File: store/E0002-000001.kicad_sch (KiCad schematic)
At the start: 27 parts, among them J1 Power_IN, J2 Connector, J3 S0 input from DIN meter, J4 Leak sensor, J5 Door reed (NO), J6 Seansor_Header_A, J7 Seansor_Header_B, U1 TMP117xxDRV, U2 INA226

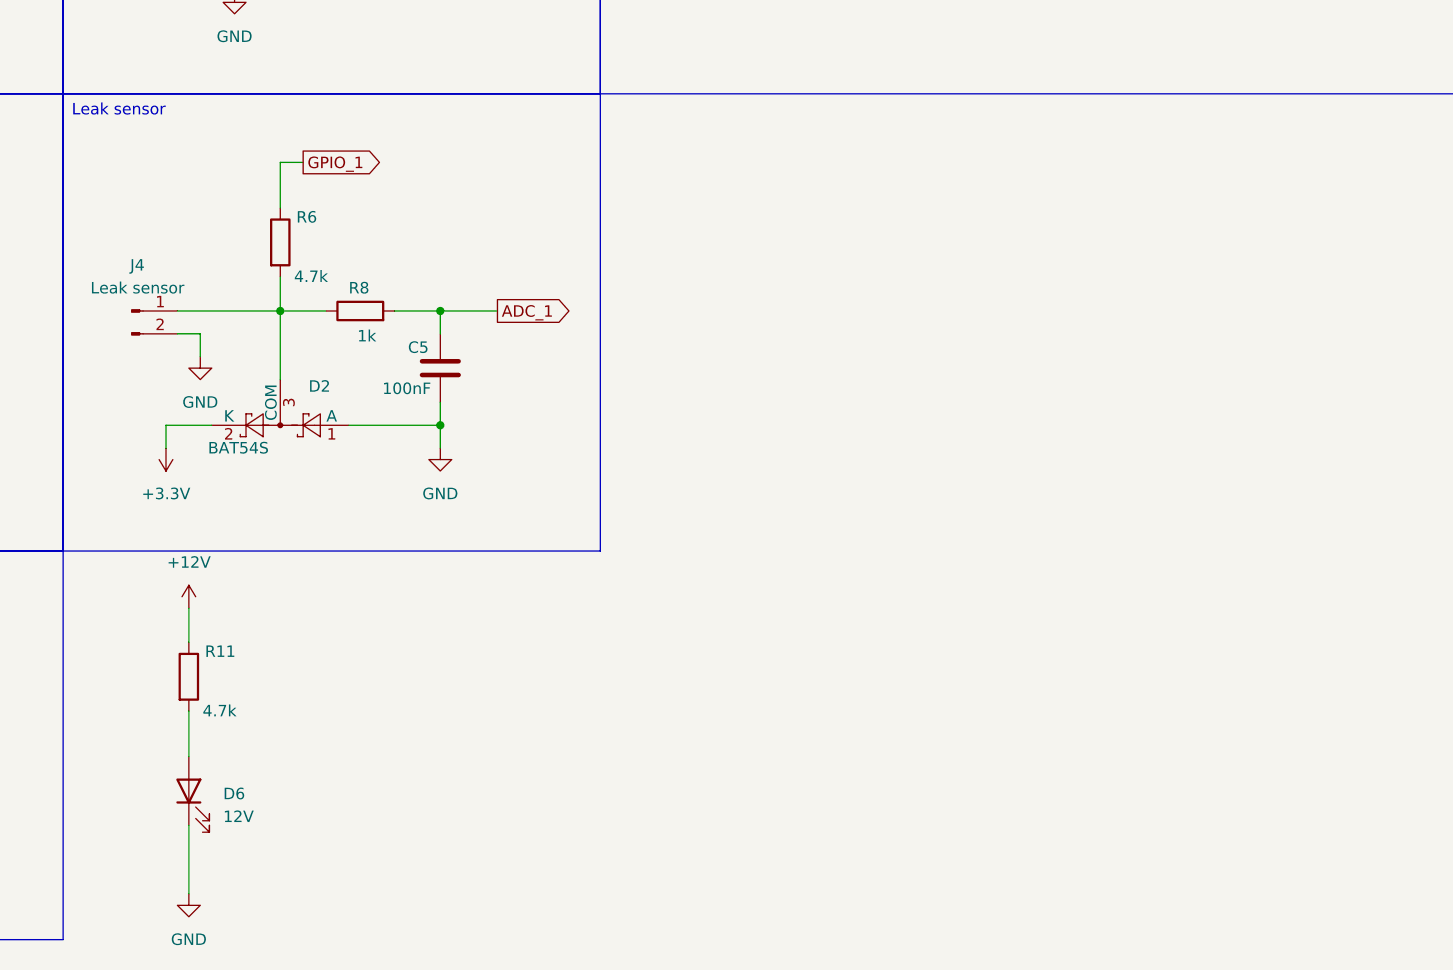
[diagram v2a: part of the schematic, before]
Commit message: feat(E0002): continue PCB layout and add footprint library table
- Update E0002 PCB layout, schematic, and project routing/designators
- Add store/fp-lib-table referencing the industrygrow footprint library
- Update active layer state in E0001/E0002 board settings

Signed-off-by: IIchukissII <133657307+IIchukissII@users.noreply.github.com>
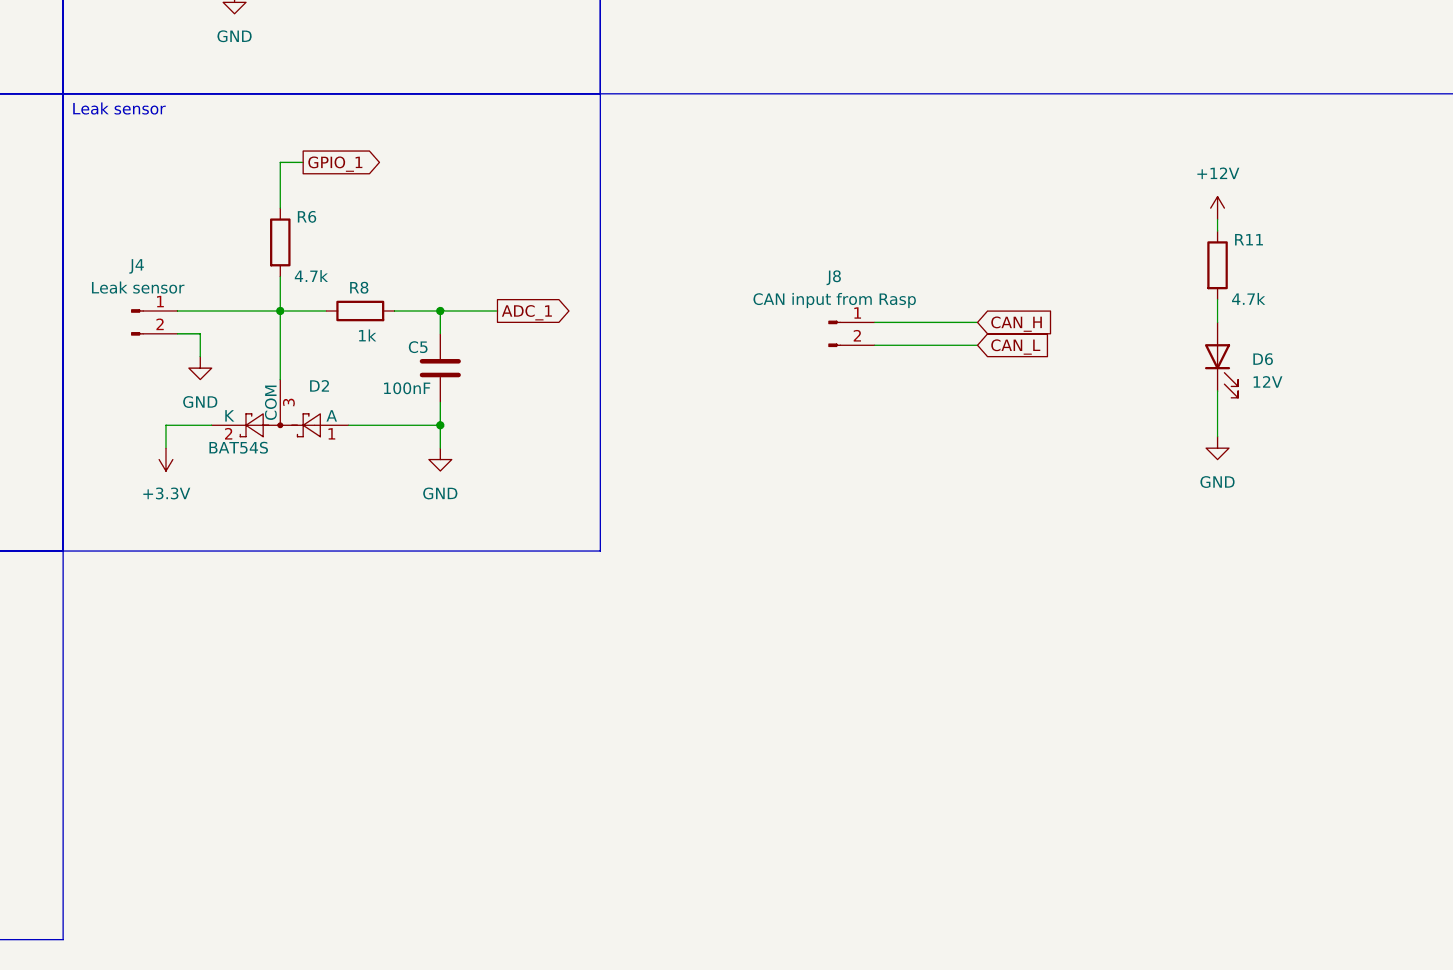
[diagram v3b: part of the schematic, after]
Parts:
- added J8: CAN input from Rasp, TerminalBlock_Phoenix:TerminalBlock_Phoenix_MKDS-1,5-2_1x02_P5.00mm_Horizontal, symbol Connector:Conn_01x02_Pin
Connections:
- net CAN_H: now also J8.1 (Pin_1)
- net CAN_L: now also J8.2 (Pin_2)
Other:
- moved on the sheet: D6, R11
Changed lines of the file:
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@@
 	(wire
 		(pts
-			(xy 133.35 147.32) (xy 133.35 152.4)
+			(xy 247.65 101.6) (xy 247.65 104.14)
 		)
 		(stroke
@@
 	(wire
 		(pts
-			(xy 133.35 135.89) (xy 133.35 139.7)
+			(xy 247.65 92.71) (xy 247.65 93.98)
 		)
 		(stroke
@@
 	(wire
 		(pts
+			(xy 209.55 104.14) (xy 220.98 104.14)
+		)
+		(stroke
+			(width 0)
+			(type default)
+		)
+	)
+	(wire
+		(pts
 			(xy 82.55 153.67) (xy 92.71 153.67)
 		)
@@
 	(wire
 		(pts
-			(xy 133.35 160.02) (xy 133.35 167.64)
+			(xy 247.65 111.76) (xy 247.65 116.84)
 		)
 		(stroke
@@
 	(wire
 		(pts
+			(xy 209.55 106.68) (xy 220.98 106.68)
+		)
+		(stroke
+			(width 0)
+			(type default)
+		)
+	)
+	(wire
+		(pts
 			(xy 81.28 25.4) (xy 81.28 26.67)
 		)
@@
 		)
 	)
+	(global_label "CAN_L"
+		(shape input)
+		(at 220.98 106.68 0)
+		(fields_autoplaced yes)
+		(effects
+			(font
+				(size 1.27 1.27)
+			)
+			(justify left)
+		)
+		(property "Intersheetrefs" "${INTERSHEET_REFS}"
+			(at 229.65 106.68 0)
+			(hide yes)
+			(show_name no)
+			(do_not_autoplace no)
+			(effects
+				(font
+					(size 1.27 1.27)
+				)
+				(justify left)
+			)
+		)
+	)
 	(global_label "I2C1_SDA"
 		(shape output)
@@
 		)
 	)
+	(global_label "CAN_H"
+		(shape input)
+		(at 220.98 104.14 0)
+		(fields_autoplaced yes)
+		(effects
+			(font
+				(size 1.27 1.27)
+			)
+			(justify left)
+		)
+		(property "Intersheetrefs" "${INTERSHEET_REFS}"
+			(at 229.9524 104.14 0)
+			(hide yes)
+			(show_name no)
+			(do_not_autoplace no)
+			(effects
+				(font
+					(size 1.27 1.27)
+				)
+				(justify left)
+			)
+		)
+	)
 	(global_label "I2C1_SCL"
 		(shape output)
@@
 	)
 	(symbol
+		(lib_id "Connector:Conn_01x02_Pin")
+		(at 204.47 104.14 0)
+		(unit 1)
+		(body_style 1)
+		(exclude_from_sim no)
+		(in_bom yes)
+		(on_board yes)
+		(in_pos_files yes)
+		(dnp no)
+		(fields_autoplaced yes)
+		(property "Reference" "J8"
+			(at 205.105 99.06 0)
+			(show_name no)
+			(do_not_autoplace no)
+			(effects
+				(font
+					(size 1.27 1.27)
+				)
+			)
+		)
+		(property "Value" "CAN input from Rasp"
+			(at 205.105 101.6 0)
+			(show_name no)
+			(do_not_autoplace no)
+			(effects
+				(font
+					(size 1.27 1.27)
+				)
+			)
+		)
+		(property "Footprint" "TerminalBlock_Phoenix:TerminalBlock_Phoenix_MKDS-1,5-2_1x02_P5.00mm_Horizontal"
+			(at 204.47 104.14 0)
+			(hide yes)
+			(show_name no)
+			(do_not_autoplace no)
+			(effects
+				(font
+					(size 1.27 1.27)
+				)
+			)
+		)
+		(property "Datasheet" ""
+			(at 204.47 104.14 0)
+			(hide yes)
+			(show_name no)
+			(do_not_autoplace no)
+			(effects
+				(font
+					(size 1.27 1.27)
+				)
+			)
+		)
+		(property "Description" "Generic connector, single row, 01x02, script generated"
+			(at 204.47 104.14 0)
+			(hide yes)
+			(show_name no)
+			(do_not_autoplace no)
+			(effects
+				(font
+					(size 1.27 1.27)
+				)
+			)
+		)
+		(pin "1"
+		)
+		(pin "2"
+		)
+		(instances
+			(project "E0002-000001"
+				(path "/05ff86a2-bfad-446c-a3c5-38b9f5c2eac9"
+					(reference "J8")
+					(unit 1)
+				)
+			)
+		)
+	)
+	(symbol
 		(lib_id "Device:R")
 		(at 143.51 95.25 0)
@@
 	(symbol
 		(lib_id "Device:R")
-		(at 133.35 143.51 0)
+		(at 247.65 97.79 0)
 		(unit 1)
 		(body_style 1)
@@
 		(dnp no)
 		(property "Reference" "R11"
-			(at 135.128 140.716 0)
+			(at 249.428 94.996 0)
 			(show_name no)
 			(do_not_autoplace no)
@@
 		)
 		(property "Value" "4.7k"
-			(at 134.874 147.32 0)
+			(at 249.174 101.6 0)
 			(show_name no)
 			(do_not_autoplace no)
@@
 		)
 		(property "Footprint" "Resistor_SMD:R_0805_2012Metric"
-			(at 131.572 143.51 90)
+			(at 245.872 97.79 90)
 			(hide yes)
 			(show_name no)
@@
 		)
 		(property "Datasheet" ""
-			(at 133.35 143.51 0)
+			(at 247.65 97.79 0)
 			(hide yes)
 			(show_name no)
@@
 		)
 		(property "Description" "Resistor"
-			(at 133.35 143.51 0)
+			(at 247.65 97.79 0)
 			(hide yes)
 			(show_name no)
@@
 	(symbol
 		(lib_id "power:GND")
-		(at 133.35 167.64 0)
+		(at 247.65 116.84 0)
 		(unit 1)
 		(body_style 1)
@@
 		(fields_autoplaced yes)
 		(property "Reference" "#PWR035"
-			(at 133.35 173.99 0)
+			(at 247.65 123.19 0)
 			(hide yes)
 			(show_name no)
@@
 		)
 		(property "Value" "GND"
-			(at 133.35 172.72 0)
+			(at 247.65 121.92 0)
 			(show_name no)
 			(do_not_autoplace no)
@@
 		)
 		(property "Footprint" ""
-			(at 133.35 167.64 0)
+			(at 247.65 116.84 0)
 			(hide yes)
 			(show_name no)
@@
 		)
 		(property "Datasheet" ""
-			(at 133.35 167.64 0)
+			(at 247.65 116.84 0)
 			(hide yes)
 			(show_name no)
@@
 		)
 		(property "Description" "Power symbol creates a global label with name \"GND\" , ground"
-			(at 133.35 167.64 0)
+			(at 247.65 116.84 0)
 			(hide yes)
 			(show_name no)
@@
 	(symbol
 		(lib_id "Device:LED")
-		(at 133.35 156.21 90)
+		(at 247.65 107.95 90)
 		(unit 1)
 		(body_style 1)
@@
 		(fields_autoplaced yes)
 		(property "Reference" "D6"
-			(at 137.16 156.5274 90)
+			(at 251.46 108.2674 90)
 			(show_name no)
 			(do_not_autoplace no)
@@
 		)
 		(property "Value" "12V"
-			(at 137.16 159.0674 90)
+			(at 251.46 110.8074 90)
 			(show_name no)
 			(do_not_autoplace no)
@@
 		)
 		(property "Footprint" "LED_SMD:LED_0805_2012Metric"
-			(at 133.35 156.21 0)
+			(at 247.65 107.95 0)
 			(hide yes)
 			(show_name no)
@@
 		)
 		(property "Datasheet" ""
-			(at 133.35 156.21 0)
+			(at 247.65 107.95 0)
 			(hide yes)
 			(show_name no)
@@
 		)
 		(property "Description" "Light emitting diode"
-			(at 133.35 156.21 0)
+			(at 247.65 107.95 0)
 			(hide yes)
 			(show_name no)
@@
 		)
 		(property "Sim.Pins" "1=K 2=A"
-			(at 133.35 156.21 0)
+			(at 247.65 107.95 0)
 			(hide yes)
 			(show_name no)
@@
 	(symbol
 		(lib_id "power:+12V")
-		(at 133.35 135.89 0)
+		(at 247.65 92.71 0)
 		(unit 1)
 		(body_style 1)
@@
 		(fields_autoplaced yes)
 		(property "Reference" "#PWR033"
-			(at 133.35 139.7 0)
+			(at 247.65 96.52 0)
 			(hide yes)
 			(show_name no)
@@
 		)
 		(property "Value" "+12V"
-			(at 133.35 130.81 0)
+			(at 247.65 87.63 0)
 			(show_name no)
 			(do_not_autoplace no)
@@
 		)
 		(property "Footprint" ""
-			(at 133.35 135.89 0)
+			(at 247.65 92.71 0)
 			(hide yes)
 			(show_name no)
@@
 		)
 		(property "Datasheet" ""
-			(at 133.35 135.89 0)
+			(at 247.65 92.71 0)
 			(hide yes)
 			(show_name no)
@@
 		)
 		(property "Description" "Power symbol creates a global label with name \"+12V\""
-			(at 133.35 135.89 0)
+			(at 247.65 92.71 0)
 			(hide yes)
 			(show_name no)

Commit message: feat(E0002): continue PCB layout and add GND on schematic
Signed-off-by: IIchukissII <133657307+IIchukissII@users.noreply.github.com>
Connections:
- net +3.3V: no longer U2.7 (GND)
- net GND: now also U2.7 (GND)
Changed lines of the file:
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@@
 	(wire
 		(pts
-			(xy 81.28 64.77) (xy 95.25 64.77)
-		)
-		(stroke
-			(width 0)
-			(type default)
-		)
-	)
-	(wire
-		(pts
 			(xy 91.44 48.26) (xy 102.87 48.26)
 		)
@@
 	(wire
 		(pts
-			(xy 81.28 58.42) (xy 81.28 64.77)
+			(xy 81.28 58.42) (xy 81.28 67.31)
 		)
 		(stroke
@@
 					(unit 1)
 				)
+			)
+		)
+	)
+	(symbol
+		(lib_id "power:GND")
+		(at 81.28 67.31 0)
+		(unit 1)
+		(body_style 1)
+		(exclude_from_sim no)
+		(in_bom yes)
+		(on_board yes)
+		(in_pos_files yes)
+		(dnp no)
+		(fields_autoplaced yes)
+		(property "Reference" "#PWR030"
+			(at 81.28 73.66 0)
+			(hide yes)
+			(show_name no)
+			(do_not_autoplace no)
+			(effects
+				(font
+					(size 1.27 1.27)
+				)
+			)
+		)
+		(property "Value" "GND"
+			(at 81.28 72.39 0)
+			(show_name no)
+			(do_not_autoplace no)
+			(effects
+				(font
+					(size 1.27 1.27)
+				)
+			)
+		)
+		(property "Footprint" ""
+			(at 81.28 67.31 0)
+			(hide yes)
+			(show_name no)
+			(do_not_autoplace no)
+			(effects
+				(font
+					(size 1.27 1.27)
+				)
+			)
+		)
+		(property "Datasheet" ""
+			(at 81.28 67.31 0)
+			(hide yes)
+			(show_name no)
+			(do_not_autoplace no)
+			(effects
+				(font
+					(size 1.27 1.27)
+				)
+			)
+		)
+		(property "Description" "Power symbol creates a global label with name \"GND\" , ground"
+			(at 81.28 67.31 0)
+			(hide yes)
+			(show_name no)
+			(do_not_autoplace no)
+			(effects
+				(font
+					(size 1.27 1.27)
+				)
+			)
+		)
+		(pin "1"
+		)
+		(instances
+			(project "E0002-000001"
+				(path "/05ff86a2-bfad-446c-a3c5-38b9f5c2eac9"
+					(reference "#PWR030")
+					(unit 1)
+				)
